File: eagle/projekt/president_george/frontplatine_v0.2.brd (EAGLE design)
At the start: 192 x 48 mm, 141 parts, among them IC1 MEGA128-A, IC2 LM393D, IC3 TLC59116, IC4 TLC59116, IC5 PCA9555D, IC6 PCA9555D, IC7 25LC080SN, IC8 PCF8576, IC9 ISL95811UFUZ, Q1 Farnell: 1640903RL, SW22 ROTARY_SWITCH, T1 PZT2222A, T4 PZT2222A, T5 BCX19SMD, T6 BCX19SMD, X1 52207-1085, X2 Goldcap, X3 I/O, X4 I2C, X5 PTT/+-, X6 52207-1085, X7 52207-1085

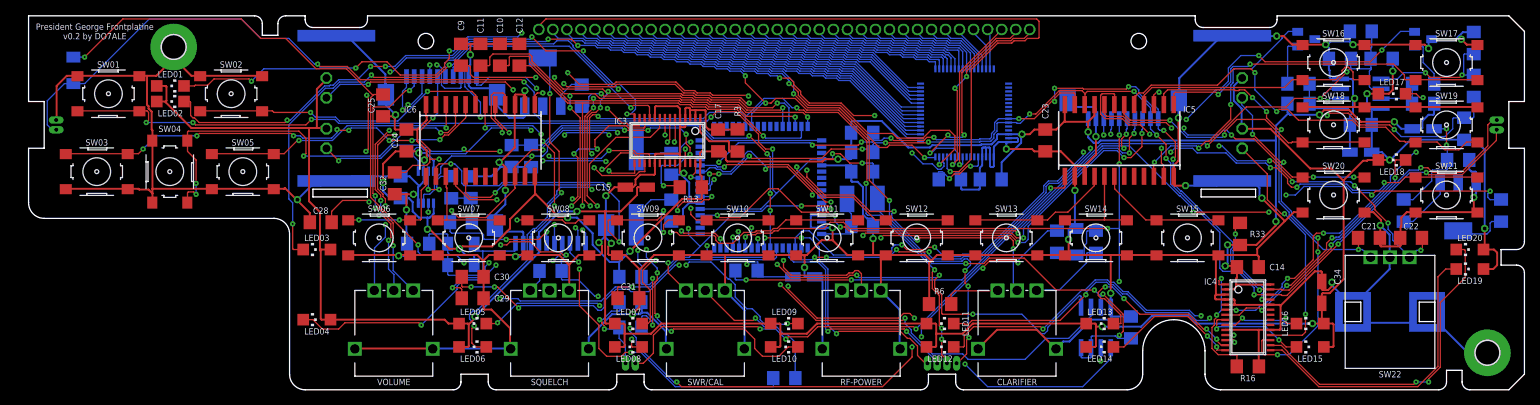
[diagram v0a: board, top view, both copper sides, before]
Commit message: - deleted wrong netclass von frontplatine
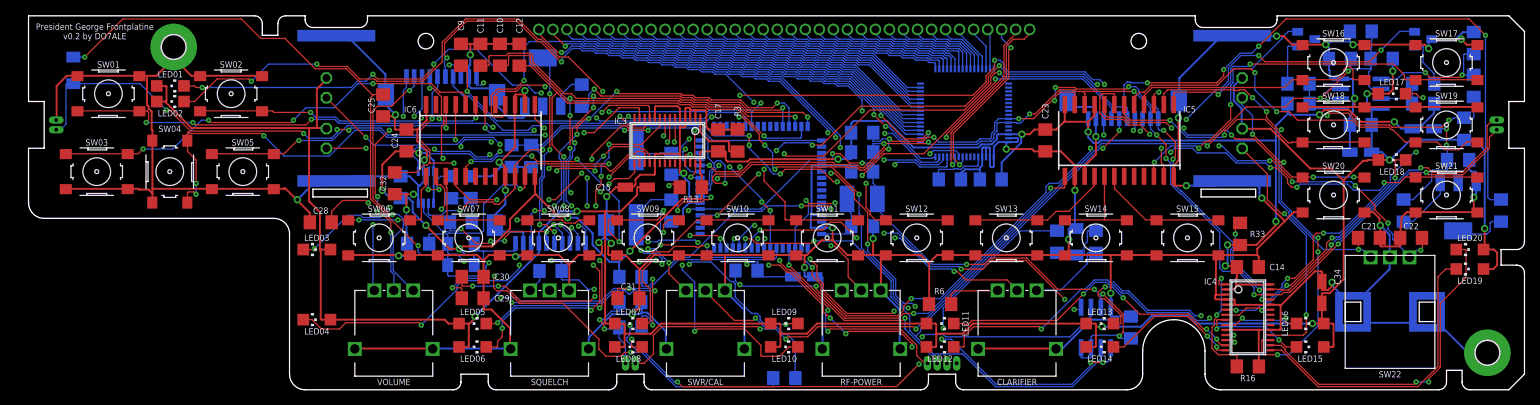
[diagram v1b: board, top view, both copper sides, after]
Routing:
- net N$1: track 94.6 -> 62.4 mm, vias 1 -> 3
- net N$69: track 137.2 -> 110.3 mm, vias 12 -> 6
- net VCCMEM: track 203.3 -> 182.1 mm, vias 10 -> 12
- net RST: track 124.0 -> 143.4 mm, vias 11 -> 8
- net N$40: track 73.1 -> 54.3 mm, vias 4 -> 5
- net SCK: track 84.4 -> 99.2 mm, vias 6 -> 4
- net SCL: track 189.7 -> 204.2 mm, vias 20 -> 15
- net N$11: track 99.4 -> 86.8 mm, vias 7 -> 6
- net N$109: track 58.8 -> 50.8 mm, vias 5 -> 6
- net N$127: track 73.9 -> 81.7 mm, vias 2 -> 4
- net N$70: track 108.4 -> 100.7 mm, vias 9 -> 10
- net GND: track 890.5 -> 884.4 mm
- net PDI: track 51.0 -> 57.1 mm, vias 6 -> 4
- net N$21: track 62.5 -> 56.5 mm
- net N$101: track 77.5 -> 71.6 mm
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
